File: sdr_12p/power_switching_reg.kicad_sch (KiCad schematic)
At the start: 22 parts, among them U36 ADP2302ARDZ, U37 ADP2302ARDZ

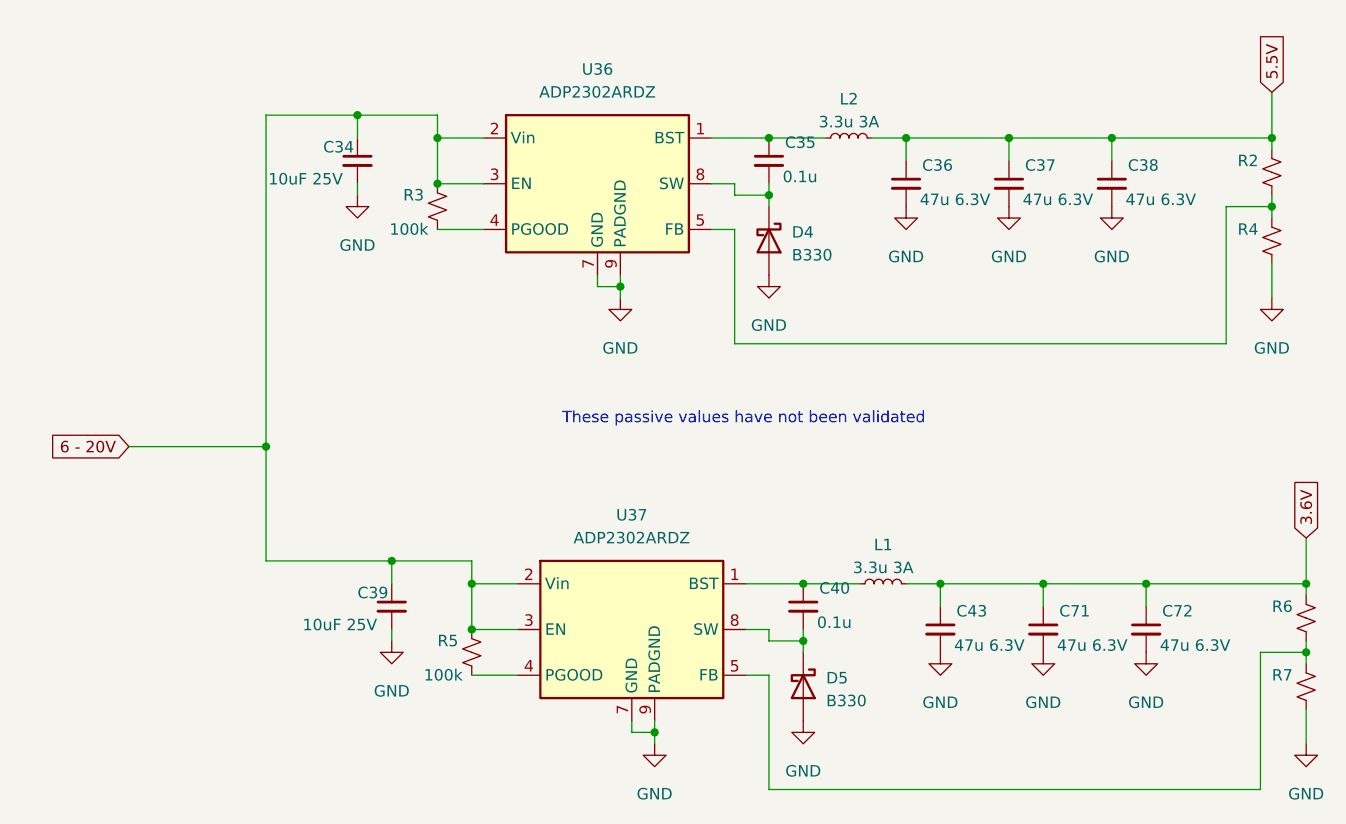
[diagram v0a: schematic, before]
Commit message: added power mgmt
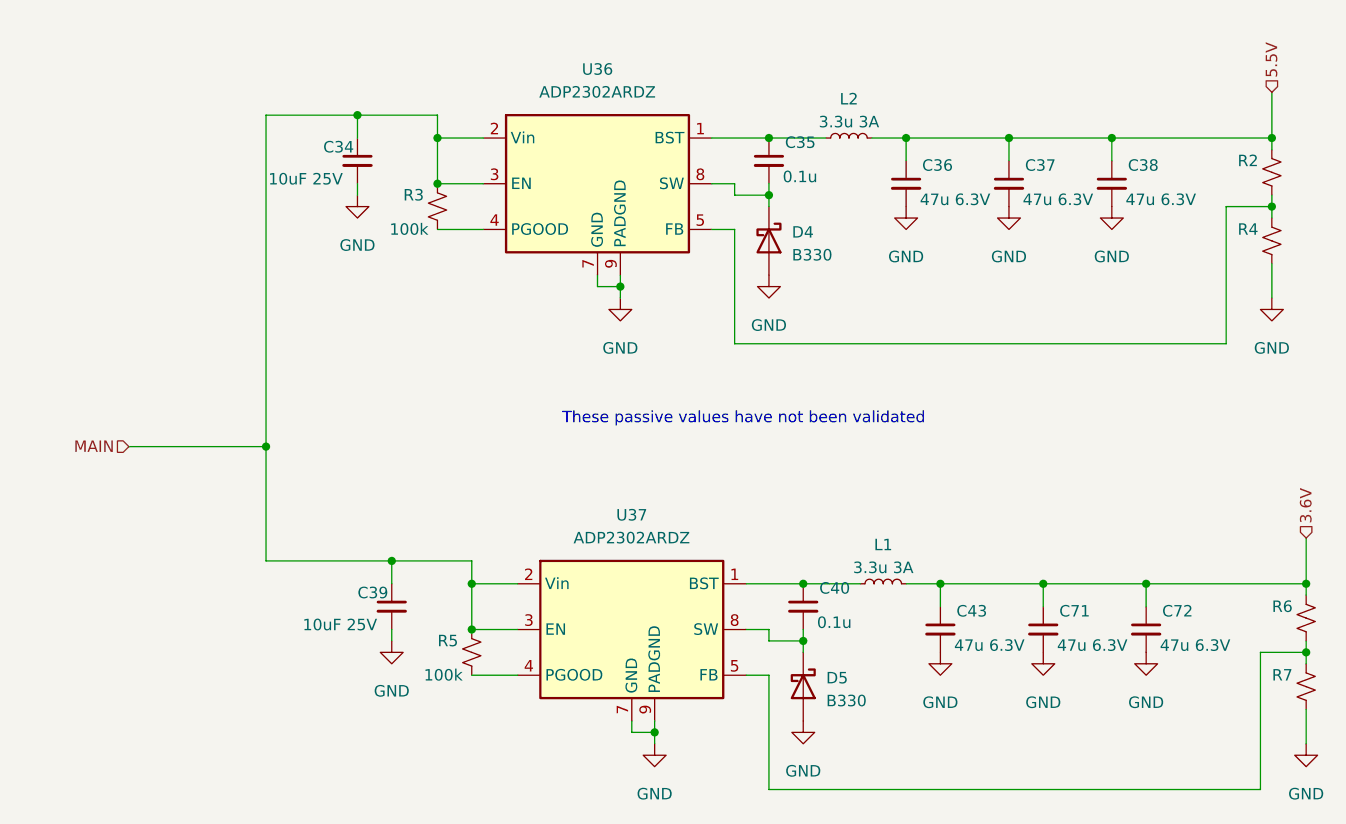
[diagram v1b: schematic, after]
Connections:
- net 6 - 20V renamed MAIN
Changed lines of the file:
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@@
 		)
 	)
-	(global_label "5.5V"
+	(hierarchical_label "MAIN"
 		(shape input)
-		(at 196.85 48.26 90)
-		(fields_autoplaced yes)
+		(at 69.85 87.63 180)
+		(effects
+			(font
+				(size 1.27 1.27)
+			)
+			(justify right)
+		)
+	)
+	(hierarchical_label "3.6V"
+		(shape input)
+		(at 200.66 97.79 90)
 		(effects
 			(font
@@
 			(justify left)
 		)
-		(property "Intersheetrefs" "${INTERSHEET_REFS}"
-			(at 196.85 41.1624 90)
-			(effects
-				(font
-					(size 1.27 1.27)
-				)
-				(justify left)
-				(hide yes)
-			)
-		)
 	)
-	(global_label "3.6V"
+	(hierarchical_label "5.5V"
 		(shape input)
-		(at 200.66 97.79 90)
-		(fields_autoplaced yes)
+		(at 196.85 48.26 90)
 		(effects
 			(font
@@
 			(justify left)
 		)
-		(property "Intersheetrefs" "${INTERSHEET_REFS}"
-			(at 200.66 90.6924 90)
-			(effects
-				(font
-					(size 1.27 1.27)
-				)
-				(justify left)
-				(hide yes)
-			)
-		)
 	)
-	(global_label "6 - 20V"
-		(shape input)
-		(at 69.85 87.63 180)
-		(fields_autoplaced yes)
-		(effects
-			(font
-				(size 1.27 1.27)
-			)
-			(justify right)
-		)
-		(property "Intersheetrefs" "${INTERSHEET_REFS}"
-			(at 58.6401 87.63 0)
-			(effects
-				(font
-					(size 1.27 1.27)
-				)
-				(justify right)
-				(hide yes)
-			)
-		)
-	)

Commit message: added uC
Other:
- company: (none) -> Andy McCann KA3KAF and Doug McCann KA3KAG
- title: (none) -> Power Switching Regulators
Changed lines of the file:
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@@
 	(generator "eeschema")
 	(generator_version "9.0")
-	(paper "A4")
+	(paper "B")
+	(title_block
+		(title "Power Switching Regulators")
+		(date "2026-01-02")
+		(rev "0.-")
+		(company "Andy McCann KA3KAF and Doug McCann KA3KAG")
+	)
 	(text "These passive values have not been validated"
 		(exclude_from_sim no)
